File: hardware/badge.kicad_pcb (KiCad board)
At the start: 2 copper layers, 88 x 115 mm, 108 parts, among them J1 Micro_SD_Card, J2 batt, J3 Conn_01x40, J4 USB_C_Receptacle_USB2.0_14P, Q1 AO3400A, Q3 AO3400A, SW1 SW_Push, SW10 SW_Push, SW11 SW_Push, SW12 SW_Push, SW13 SW_Push, SW14 SW_Push, SW15 SW_Push, SW17 SW_Push, SW18 SW_Push, SW19 SW_Push, SW2 SW_Push, SW20 SW_Push, SW21 SW_Push, SW22 SW_Push, SW23 SW_Push, SW25 SW_Push, SW26 SW_Push, SW27 SW_Push, SW28 SW_Push, SW29 SW_Push, SW3 SW_Push, SW30 SW_Push, SW31 SW_Push, SW33 SW_Push, SW34 SW_Push, SW35 SW_Push, SW36 SW_Push, SW37 SW_Push, SW38 SW_Push, SW39 SW_Push, SW4 SW_Push, SW5 SW_Push, SW57 MK-12C02-G020, SW58 SKRHABE010, SW6 SW_Push, SW7 SW_Push, SW8 BOOT, SW9 SW_Push, U1 ESP32-S3-WROOM-1, U2 74HC138, U3 BQ24075RGT, U4 TLV62569DBV, U5 BME280, U6 USBLC6-2P6, U7 BMI270, U8 Ai-Thinker-Ra-02

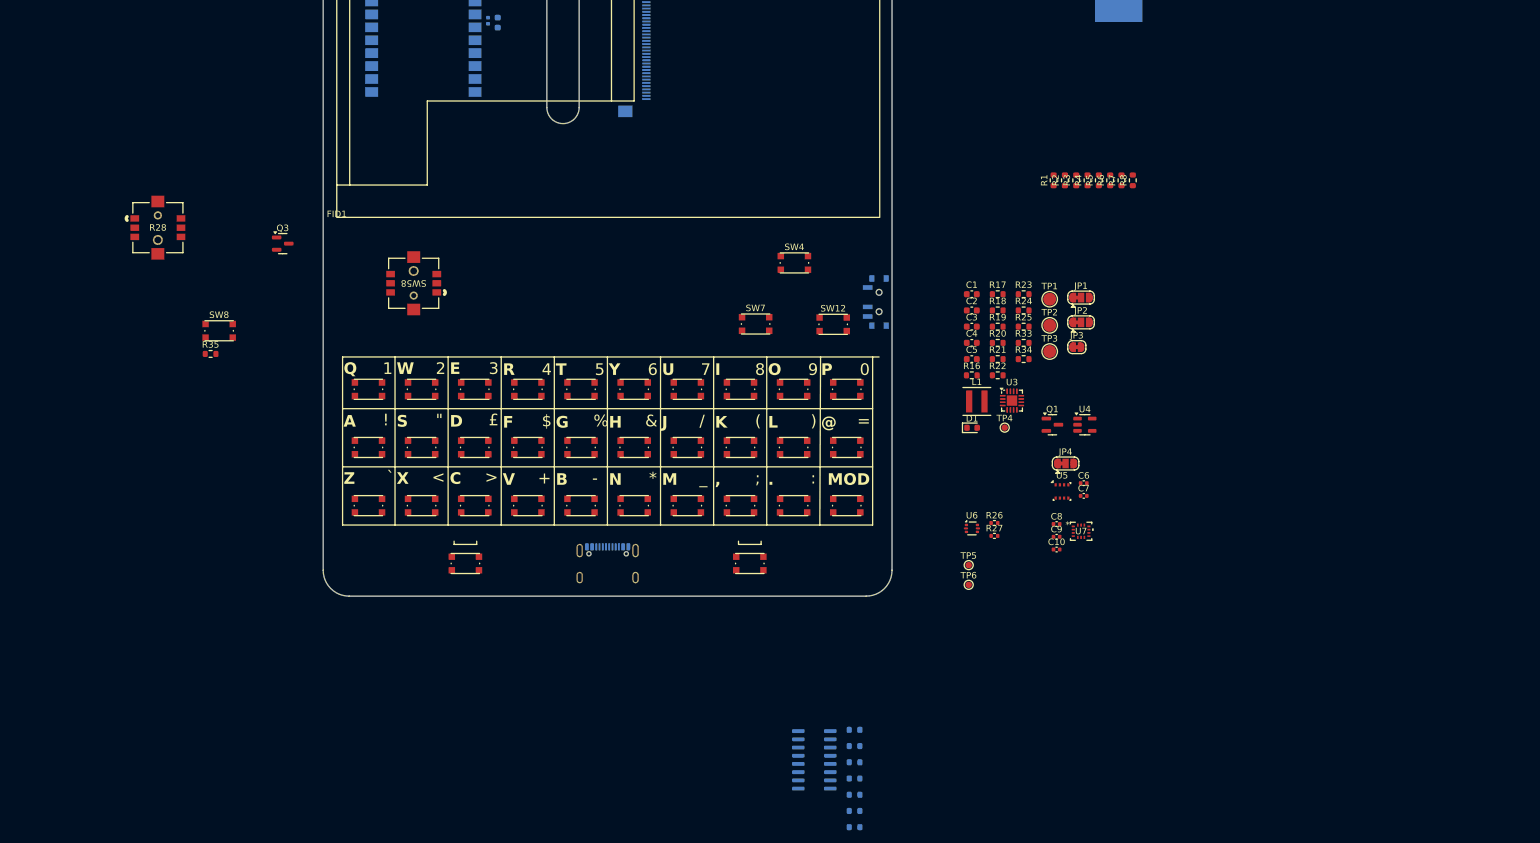
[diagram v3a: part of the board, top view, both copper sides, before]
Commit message: group things in layout
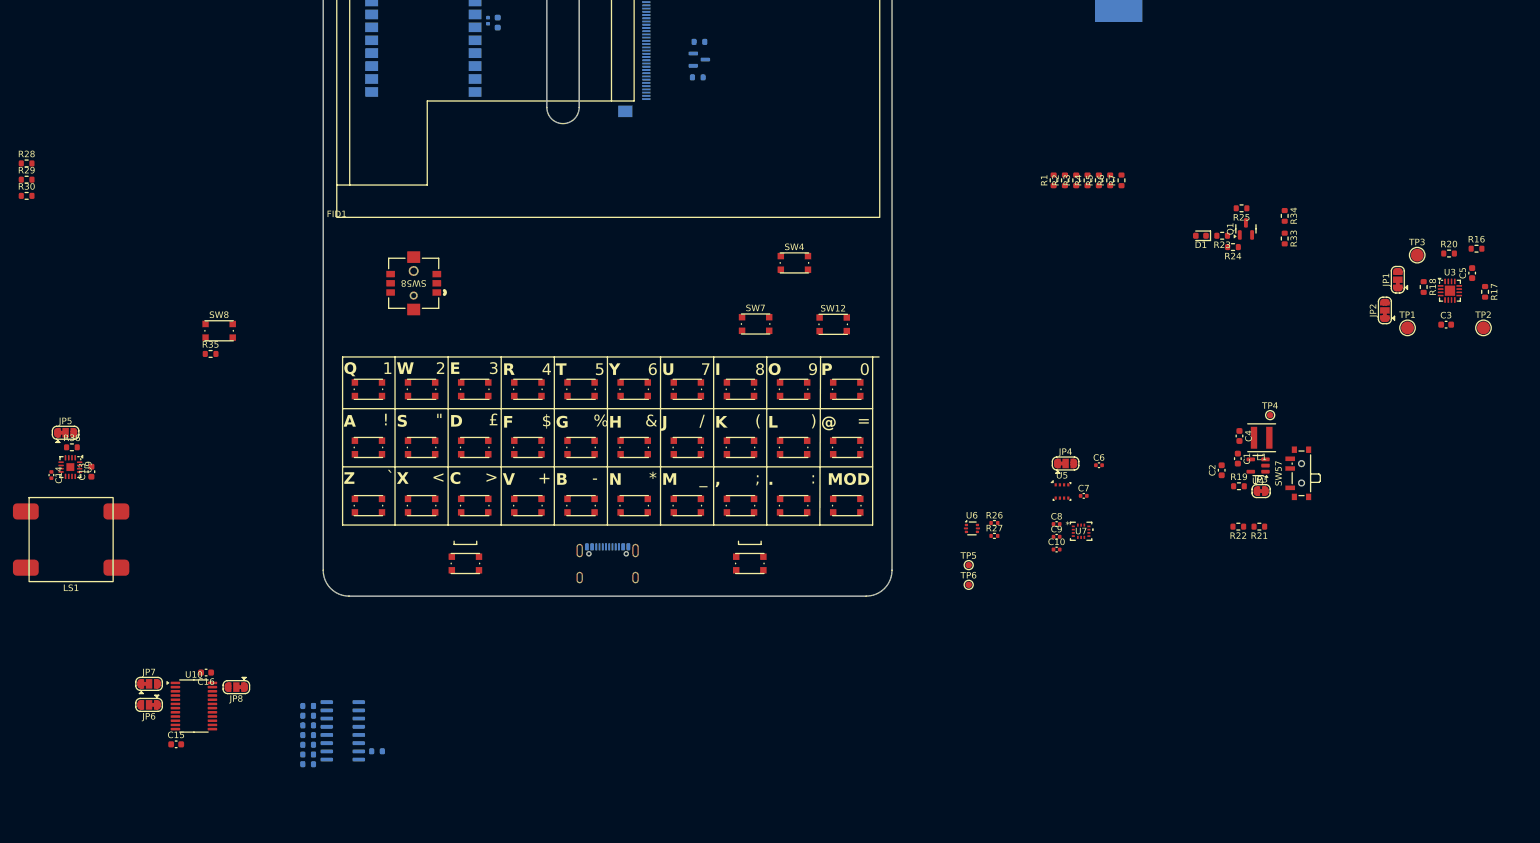
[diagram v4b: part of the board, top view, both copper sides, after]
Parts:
- added C13: 10uF, Capacitor_SMD:C_0603_1608Metric, F.Cu at (45.1, 126.8)
- added C14: 100nF, Capacitor_SMD:C_0402_1005Metric, F.Cu at (39.0, 127.3)
- added C15: 10uF, Capacitor_SMD:C_0603_1608Metric, F.Cu at (58.3, 168.9)
- added C16: 10uF, Capacitor_SMD:C_0603_1608Metric, F.Cu at (62.9, 157.8)
- added JP5: EN1, Jumper:SolderJumper-3_P1.3mm_Bridged12_RoundedPad1.0x1.5mm, F.Cu at (41.1, 120.7)
- added JP6: SolderJumper_3_Bridged12, Jumper:SolderJumper-3_P1.3mm_Bridged12_RoundedPad1.0x1.5mm, F.Cu at (54.1, 162.8)
- added JP7: SolderJumper_3_Bridged12, Jumper:SolderJumper-3_P1.3mm_Bridged12_RoundedPad1.0x1.5mm, F.Cu at (54.1, 159.6)
- added JP8: SolderJumper_3_Bridged12, Jumper:SolderJumper-3_P1.3mm_Bridged12_RoundedPad1.0x1.5mm, F.Cu at (67.6, 160.1)
- added LS1: 8Ω@1W, lib:KLJ-01304T-08R07W, F.Cu at (42.0, 137.2)
- added R29: 0R, Resistor_SMD:R_0603_1608Metric, F.Cu at (35.1, 81.6)
- added R30: 0R, Resistor_SMD:R_0603_1608Metric, F.Cu at (35.1, 84.1)
- added R31: 100R, Resistor_SMD:R_0603_1608Metric, B.Cu at (138.9, 65.8)
- added R32: 12R, Resistor_SMD:R_0603_1608Metric, B.Cu at (139.2, 60.2)
- added R36: 0R, Resistor_SMD:R_0603_1608Metric, F.Cu at (42.1, 123.0)
- added U10: PCA9555PW, Package_SO:TSSOP-24_4.4x7.8mm_P0.65mm, F.Cu at (61.0, 163.0)
- added U9: MAX98357A, Package_DFN_QFN:TQFN-16-1EP_3x3mm_P0.5mm_EP1.23x1.23mm, F.Cu at (41.9, 126.0)
- Q3, R8: moved to B.Cu
- R28: footprint lib:SKRHABE010_ALPS -> Resistor_SMD:R_0603_1608Metric
- SW57: moved to F.Cu
- moved R8 151.3 mm to (78.7, 163.0), turned to 180 degrees
- moved R14 84.8 mm to (78.7, 172.0)
- moved R13 84.8 mm to (78.7, 170.5)
- moved R12 84.7 mm to (78.7, 169.0)
- moved R11 84.6 mm to (78.7, 167.5), turned to 0 degrees
- moved R10 84.6 mm to (78.7, 166.0)
- moved R9 84.6 mm to (78.7, 164.5)
- moved R16 80.5 mm to (259.4, 92.2)
- moved C5 78.5 mm to (258.8, 96.0), turned to 90 degrees
- moved R17 75.4 mm to (260.8, 98.9), turned to -90 degrees
- moved R15 74.8 mm to (89.3, 170.0), turned to 0 degrees
- moved C3 73.4 mm to (254.7, 104.0)
- moved U2 73.1 mm to (84.0, 166.8)
- moved R20 71.2 mm to (255.2, 93.0)
- moved SW57 70.5 mm to (232.0, 127.0), turned to 90 degrees
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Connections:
- TP6 pad 1: /imu/SDA -> /imu/SCL
- U1 pad 12: /keyboard/KB_COL0 -> unconnected-(U1-IO8-Pad12)
- U1 pad 17: /keyboard/KB_COL1 -> unconnected-(U1-IO9-Pad17)
- U1 pad 18: /keyboard/KB_COL2 -> unconnected-(U1-IO10-Pad18)
- U1 pad 19: /keyboard/KB_COL3 -> unconnected-(U1-IO11-Pad19)
- U1 pad 20: /keyboard/KB_COL4 -> /AUDIO.SD
- U1 pad 21: unconnected-(U1-IO13-Pad21) -> /AUDIO.LRCLK
- U1 pad 22: unconnected-(U1-IO14-Pad22) -> /AUDIO.BCLK
- U1 pad 23: GND -> unconnected-(U1-IO21-Pad23)
- U1 pad 24: /imu/SDA -> /imu/SCL
- U1 pad 25: /imu/SCL -> Net-(U1-IO48)
- U1 pad 34: /lcd/SPI_CS -> unconnected-(U1-IO41-Pad34)
- U1 pad 35: /lcd/BACKLIGHT -> Net-(U1-IO42)
- U1 pad 5: /keyboard/KB_ROW0 -> unconnected-(U1-IO5-Pad5)
- U1 pad 6: /keyboard/KB_ROW1 -> unconnected-(U1-IO6-Pad6)
- U1 pad 7: /keyboard/KB_ROW2 -> unconnected-(U1-IO7-Pad7)
- U1 pad 8: /mcu/LORA_CE -> unconnected-(U1-IO15-Pad8)
- U1 pad 9: /mcu/LORA_NSS -> unconnected-(U1-IO16-Pad9)
- U5 pad 3: /imu/SDA -> /imu/SCL
- U7 pad 14: /imu/SDA -> /imu/SCL

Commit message: Bms routing (#16)
Routhe BMS subsystem

Fix the JP1 and JP2 power net
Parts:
- C2, C3, C5, JP1, JP2, Q1, R16, R17, R18, R20, R23, R24, R33, R34, TP1, TP2, TP3, U3: moved to B.Cu
- R28: footprint Resistor_SMD:R_0603_1608Metric -> lib:SKRHABE010_ALPS
- moved C2 82.2 mm to (207.7, 45.2)
- moved R25 74.9 mm to (235.5, 159.9)
- moved Q1 71.4 mm to (241.9, 158.2), turned to 180 degrees
- moved D1 68.2 mm to (241.5, 153.8), turned to 0 degrees
- moved R23 67.1 mm to (241.5, 153.8)
- moved R24 66.7 mm to (241.5, 155.7)
- moved TP2 66.5 mm to (223.5, 49.3), turned to 180 degrees
- moved R34 65.4 mm to (235.6, 152.3)
- moved R33 65.2 mm to (235.6, 155.6)
- moved TP1 64.4 mm to (223.5, 45.2), turned to 180 degrees
- moved JP1 59.7 mm to (245.7, 156.7)
- moved C5 58.6 mm to (244.5, 152.9), turned to -90 degrees
- moved R20 57.5 mm to (251.5, 150.4)
- moved R16 56.3 mm to (246.4, 147.0), turned to 90 degrees
- moved JP2 55.0 mm to (248.9, 156.7)
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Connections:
- J3 pad 15: GND -> /lcd/RESET
- JP1 pad 1: VDD -> VSYS
- JP2 pad 3: VDD -> VSYS
- TP6 pad 1: /imu/SCL -> /imu/SDA
- U1 pad 25: Net-(U1-IO48) -> /imu/SDA
- U10 pad 23: Net-(U1-IO48) -> /imu/SDA
- U10 pad 6: GND -> /lcd/RESET
- U5 pad 3: /imu/SCL -> /imu/SDA
- U7 pad 14: /imu/SCL -> /imu/SDA
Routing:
- net /power/~{CHG}: track 0.00 -> 8.03 mm
- net Net-(U3-ILIM): track 0.00 -> 5.74 mm, vias 0 -> 2
- net /power/EN1: track 0.00 -> 5.16 mm
- net /power/EN2: track 0.00 -> 5.10 mm
- net /power/ISET: track 0.00 -> 4.80 mm
- net GND: track 0.00 -> 3.72 mm, vias 0 -> 5
- net VSYS: track 0.00 -> 2.90 mm, vias 0 -> 11
- net Net-(U3-TMR): track 0.00 -> 2.52 mm
- net Net-(D1-K): track 0.00 -> 2.03 mm, vias 0 -> 1
- net Net-(U3-TS): track 0.00 -> 1.94 mm
- added copper zone on B.Cu, net GND
- added copper zone on B.Cu, net Net-(J2-Pin_2)
- added copper zone on B.Cu, net VSYS
- added copper zone on F.Cu, net VSYS
- added copper zone on B.Cu, net VUSB

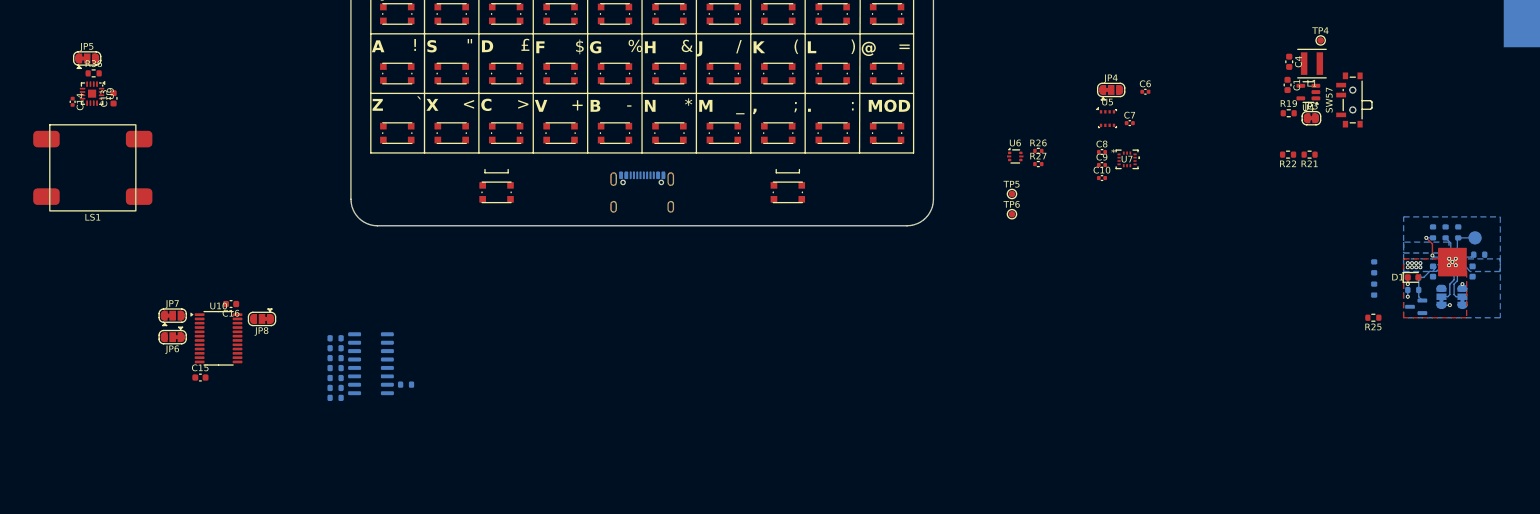
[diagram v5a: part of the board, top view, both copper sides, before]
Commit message: Route the audio subsystem
Fix BMS routing
Remove audio gain selection, to relax routing
Add DRC rule for JLC
Add custom rule for Audio BGA routing
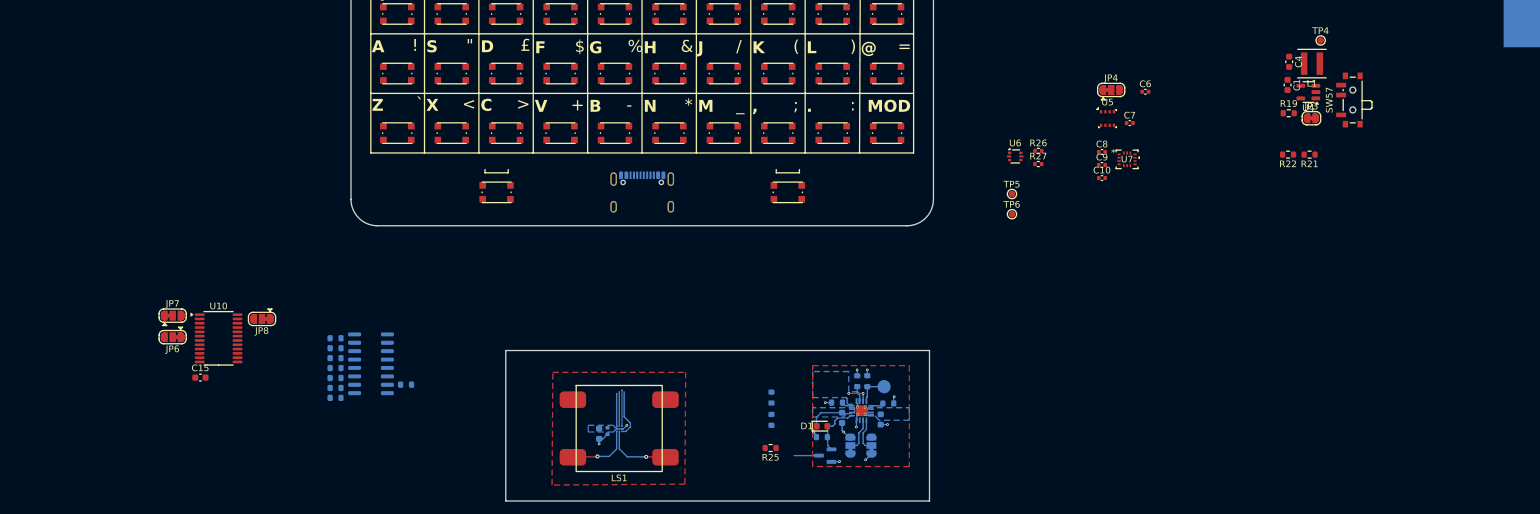
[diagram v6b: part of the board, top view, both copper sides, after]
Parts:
- removed C16: 10uF, Capacitor_SMD:C_0603_1608Metric
- removed JP5: EN1, Jumper:SolderJumper-3_P1.3mm_Bridged12_RoundedPad1.0x1.5mm
- removed R36: 0R, Resistor_SMD:R_0603_1608Metric
- C13, C14: moved to B.Cu
- U3: footprint Package_DFN_QFN:VQFN-16-1EP_3x3mm_P0.5mm_EP1.6x1.6mm -> Package_DFN_QFN:VQFN-16-1EP_3x3mm_P0.5mm_EP1.6x1.6mm_ThermalVias
- U9: footprint Package_DFN_QFN:TQFN-16-1EP_3x3mm_P0.5mm_EP1.23x1.23mm -> Package_BGA:WLP-9_1.448x1.468mm_Layout3x3_P0.4mm_Ball0.27mm_Pad0.25mm; moved to B.Cu
- moved C14 94.9 mm to (119.8, 177.0)
- moved U9 94.4 mm to (121.5, 176.7)
- moved R17 93.6 mm to (154.4, 172.7), turned to 180 degrees
- moved R25 93.2 mm to (144.4, 179.6)
- moved R33 93.2 mm to (144.5, 175.3)
- moved R34 93.2 mm to (144.5, 172.0)
- moved R23 92.5 mm to (152.1, 177.9)
- moved C3 92.2 mm to (161.0, 175.3)
- moved D1 92.1 mm to (152.2, 176.3)
- moved JP1 92.1 mm to (156.5, 179.2)
- moved Q1 92.1 mm to (152.7, 180.7)
- moved R18 92.1 mm to (159.0, 169.5)
- moved R20 92.1 mm to (162.2, 172.8)
- moved U3 92.1 mm to (158.1, 173.9)
- moved JP2 92.1 mm to (159.6, 179.2)
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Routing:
- net GND: track 3.72 -> 18.0 mm, vias 5 -> 11
- net Net-(U9-OUTN): track 0.00 -> 10.9 mm, vias 0 -> 1
- net Net-(U9-OUTP): track 0.00 -> 8.99 mm, vias 0 -> 1
- net /AUDIO.LRCLK: track 0.00 -> 7.27 mm
- net /AUDIO.BCLK: track 0.00 -> 5.47 mm
- net /AUDIO.SD: track 0.00 -> 5.21 mm
- net /mcu/MUTE: track 0.00 -> 4.96 mm
- net Net-(U3-ILIM): track 5.74 -> 1.62 mm, vias 2 -> 0
- net /mcu/CHG: track 0.00 -> 3.76 mm
- net VUSB: track 0.00 -> 3.36 mm, vias 0 -> 2
- net VSYS: track 2.90 -> 5.50 mm, vias 11 -> 0
- added copper zone on B.Cu, net +3.3V
- added copper zone on F.Cu, net GND
- removed copper zone on B.Cu, net GND
- removed copper zone on F.Cu, net VSYS
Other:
- board size 88 x 115 mm -> 88 x 156.6 mm

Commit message: Start Routing of power subsystem
Start routing of lcd and sd card, only for checking if pin swaps are
needed
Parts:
- C1, C4, JP3, L1, R19, R21, R22, R26, R27, SW57, TP4, U4, U6: moved to B.Cu
- moved J2 165.8 mm to (94.5, 101.7)
- moved Q1 104.8 mm to (164.2, 76.6), turned to 0 degrees
- moved R21 102.0 mm to (150.6, 66.3), turned to -90 degrees
- moved JP1 101.2 mm to (160.4, 78.1), turned to -90 degrees
- moved JP2 101.1 mm to (157.2, 78.1), turned to -90 degrees
- moved R23 99.4 mm to (164.7, 79.4), turned to 0 degrees
- moved R22 98.4 mm to (152.4, 66.3), turned to 90 degrees
- moved R24 96.1 mm to (164.7, 81.0), turned to 0 degrees
- moved R19 95.9 mm to (152.5, 63.6)
- moved C3 93.4 mm to (155.8, 82.0), turned to 90 degrees
- moved C5 93.0 mm to (161.7, 82.3), turned to 90 degrees
- moved JP3 92.5 mm to (165.6, 59.8), turned to 180 degrees
- moved U4 91.7 mm to (155.5, 66.8), turned to -90 degrees
- moved U3 90.6 mm to (158.7, 83.3), turned to 0 degrees
- moved SW57 89.1 mm to (166.6, 66.5), turned to -90 degrees
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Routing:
- net VUSB: track 3.36 -> 33.7 mm, vias 2 -> 3
- net /mcu/SD_CMD: track 0.00 -> 28.9 mm
- net /mcu/SD_CLK: track 0.00 -> 26.5 mm
- net /lcd/SPI_MISO: track 0.00 -> 26.4 mm
- net /lcd/SPI_MOSI: track 0.00 -> 25.7 mm
- net /lcd/SPI_CLK: track 0.00 -> 23.1 mm
- net /mcu/SD_D0: track 0.00 -> 21.7 mm
- net Net-(SW57-B): track 0.00 -> 15.7 mm, vias 0 -> 2
- net GND: track 18.0 -> 27.3 mm, vias 11 -> 77
- net Net-(D1-K): track 2.05 -> 10.3 mm
- net +3.3V: track 0.00 -> 7.47 mm, vias 0 -> 2
- net VSYS: track 5.50 -> 11.9 mm, vias 0 -> 1
- net Net-(U4-FB): track 0.00 -> 5.96 mm
- net Net-(J4-CC2): track 0.00 -> 5.88 mm
- net Net-(J4-D--PadA7): track 0.00 -> 5.88 mm
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- added copper zone on B.Cu, net /lcd/LEDK
- added copper zone on B.Cu, net GND
- added copper zone on B.Cu, net Net-(U4-SW)
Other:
- outline, holes or cut-outs redrawn

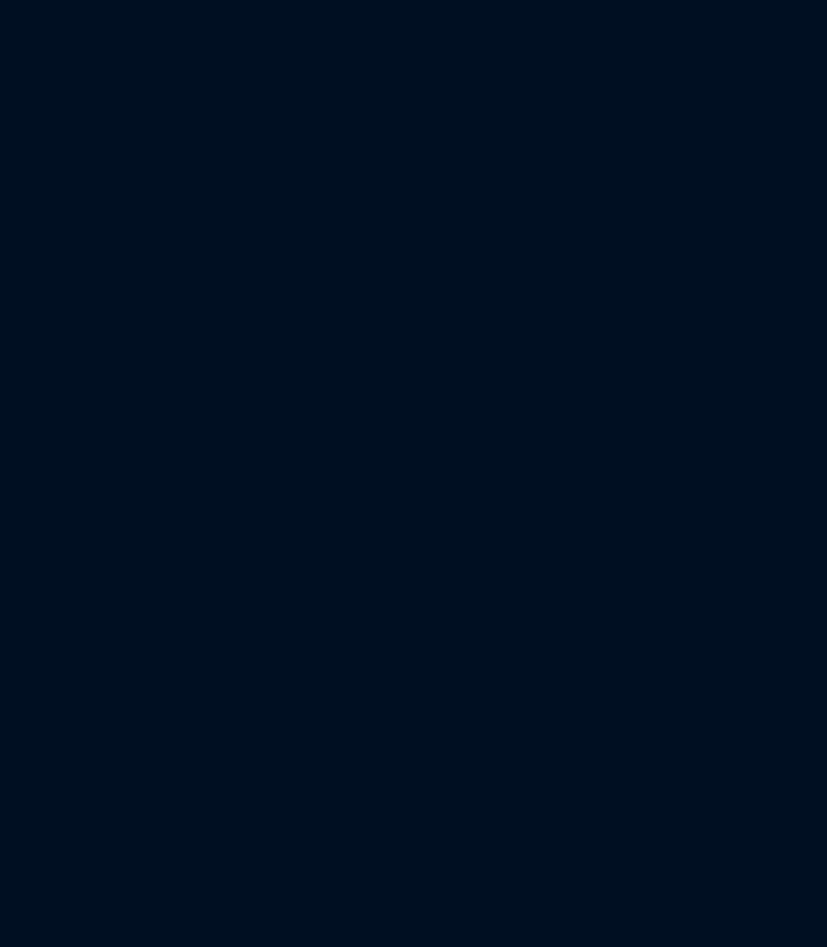
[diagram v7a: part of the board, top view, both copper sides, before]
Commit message: add adafruit joystick
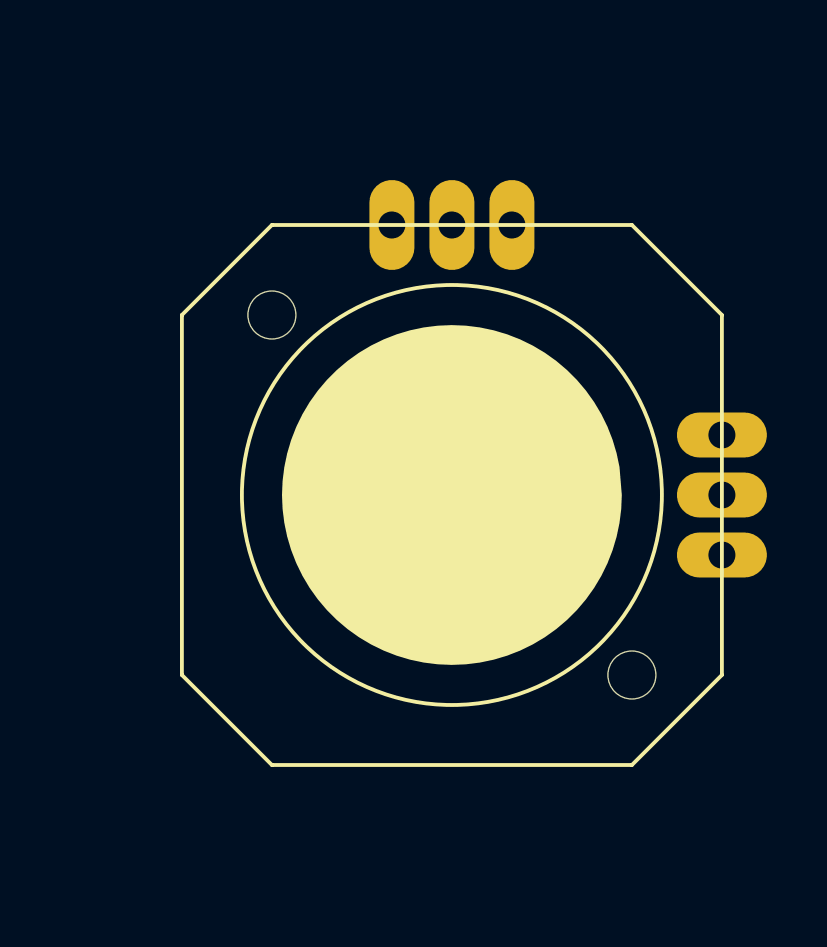
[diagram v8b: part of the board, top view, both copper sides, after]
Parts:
- added RV1: R_Potentiometer_Dual_Separate, lib:JOYSTICK_ANALOG_MINITHM, F.Cu at (223.0, 103.0)
